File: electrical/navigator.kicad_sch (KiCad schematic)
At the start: 5 parts

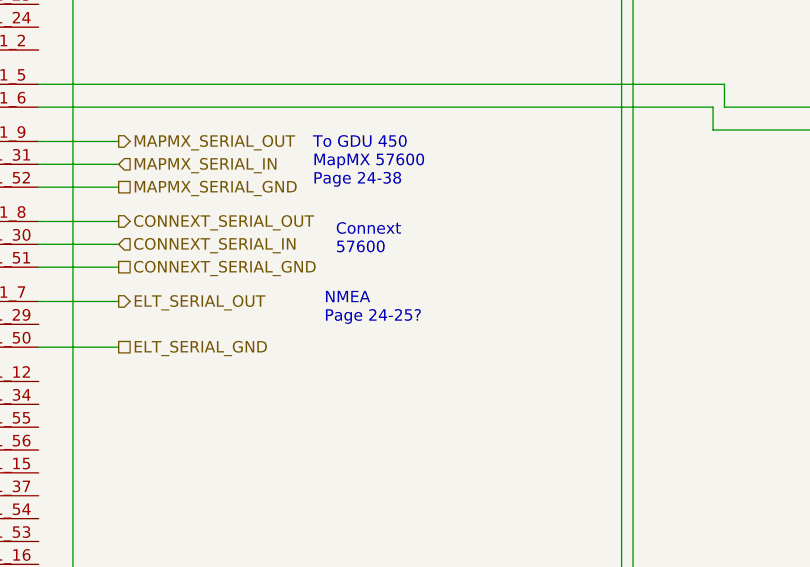
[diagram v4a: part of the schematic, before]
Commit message: Removed Amps as Rotax sends that over Can to GEA24
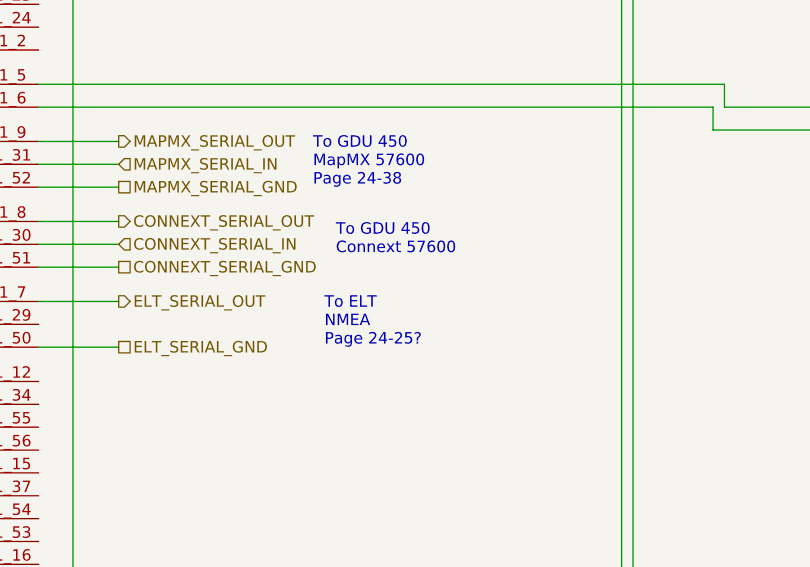
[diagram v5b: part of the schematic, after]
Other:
- note added: "To ELT NMEA Page 24-25?"
- note added: "To GDU 450 Connext 57600"
- note removed: "Connext 57600"
- note removed: "NMEA Page 24-25?"
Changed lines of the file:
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@@
     (stroke (width 0) (type default))
   )
-  (text "NMEA\nPage 24-25?" (at 96.52 95.25 0)
+  (text "To ELT\nNMEA\nPage 24-25?" (at 96.52 97.79 0)
     (effects (font (size 1.27 1.27)) (justify left bottom))
   )
@@
     (effects (font (size 1.27 1.27)) (justify left bottom))
   )
-  (text "Connext\n57600" (at 97.79 87.63 0)
+  (text "To GDU 450\nConnext 57600" (at 97.79 87.63 0)
     (effects (font (size 1.27 1.27)) (justify left bottom))
   )
